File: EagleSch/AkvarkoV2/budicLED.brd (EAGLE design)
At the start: 114.3 x 160 mm, 89 parts, among them IC1 7805T, IC2 4051N, IC3 LF33CV, IC4 ESP01, J1 TRANSFLASH-LOCK, Q1 BD243C, Q2 BD243C, Q3 BD243C, Q4 BD243C, Q5 BC546A, T1 2N5551, T2 2N5551, T3 2N5551, T4 2N5551, U1 ARDUINOR3-DIMENSION, X1 SMKDSP_1,5/2, X2 SMKDSP_1,5/8, X3 SMKDSP_1,5/3

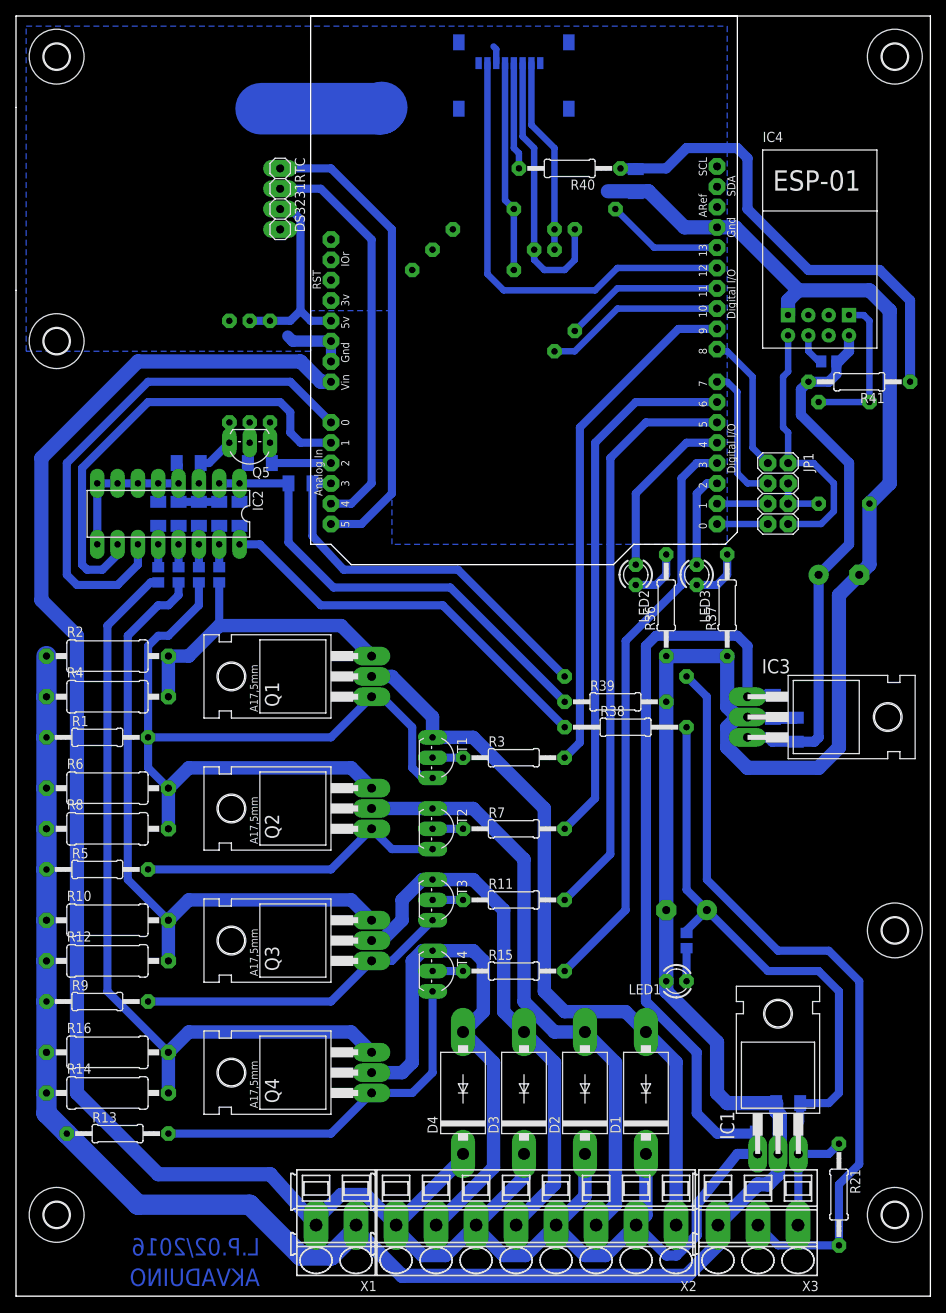
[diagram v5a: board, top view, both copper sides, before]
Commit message: DPS: - RTC modul obracen o 90°, jinak se nevejde do krabicky.
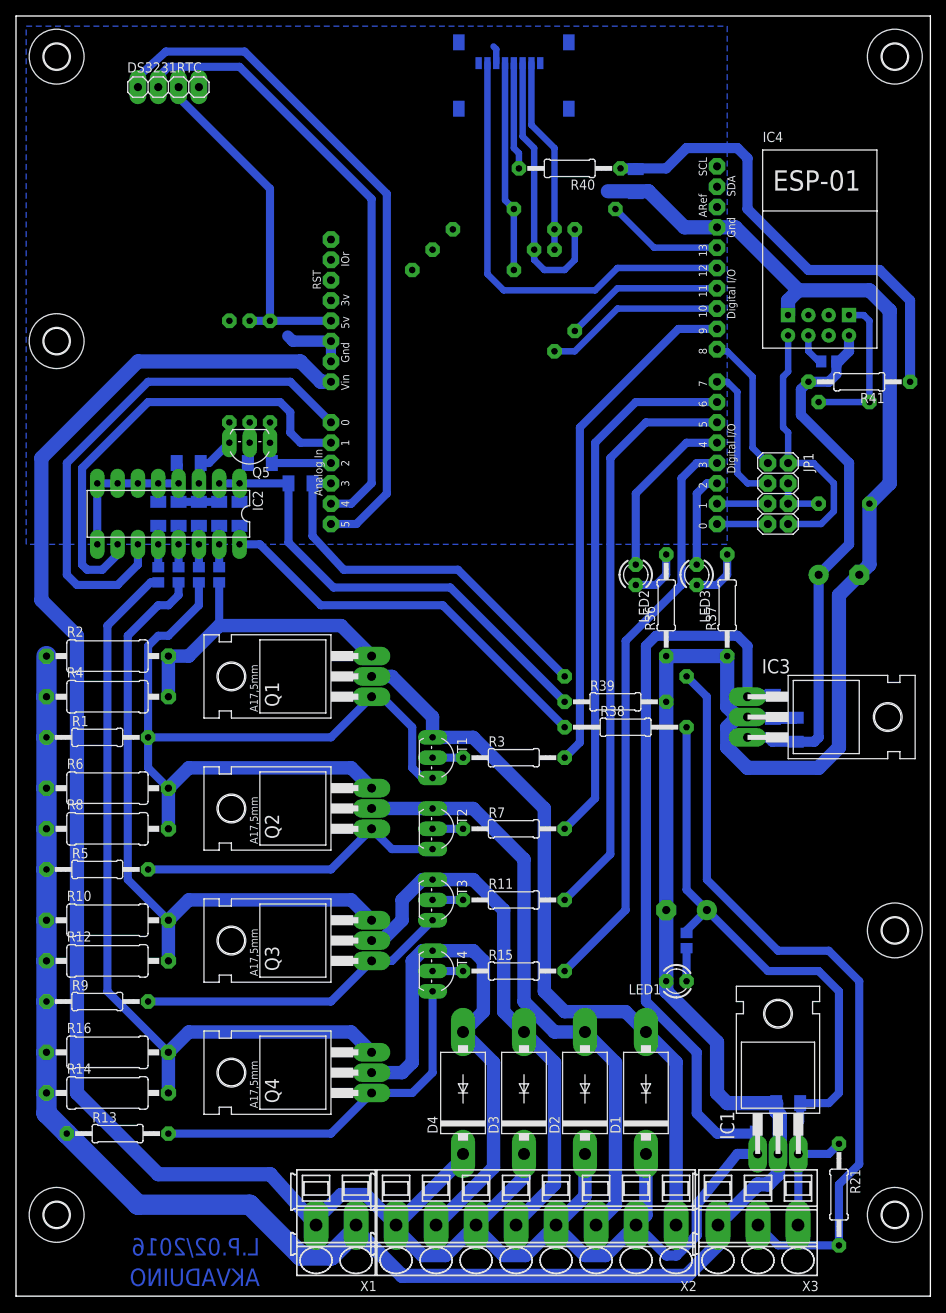
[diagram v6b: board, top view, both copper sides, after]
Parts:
- moved DS3231RTC 19.8 mm to (19.1, 151.1), turned to 0 degrees
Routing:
- net N$13: track 59.3 -> 87.0 mm
- net N$24: track 50.7 -> 77.0 mm
- net N$44: track 25.7 -> 44.1 mm
- net GND: track 412.9 -> 397.7 mm
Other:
- outline, holes or cut-outs redrawn
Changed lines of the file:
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@@
 <wire x1="114.3" y1="0" x2="114.3" y2="160.02" width="0" layer="20"/>
 <wire x1="114.3" y1="160.02" x2="0" y2="160.02" width="0" layer="20"/>
-<wire x1="0" y1="160.02" x2="0" y2="148.59" width="0" layer="20"/>
 <text x="30.48" y="5.08" size="2.1844" layer="16" font="vector" ratio="15" rot="MR0">L.P.02/2016</text>
 <text x="30.48" y="1.27" size="2.1844" layer="16" font="vector" ratio="15" rot="MR0">AKVADUINO</text>
-<wire x1="0" y1="125.73" x2="0" y2="0" width="0" layer="20"/>
-<wire x1="0" y1="125.73" x2="0" y2="148.59" width="0" layer="20"/>
+<wire x1="0" y1="160.02" x2="0" y2="0" width="0" layer="20"/>
 <dimension x1="0" y1="0" x2="114.3" y2="0" x3="57.15" y3="-8.89" textsize="1.778" layer="48"/>
 <dimension x1="114.3" y1="0" x2="114.3" y2="160.02" x3="124.46" y3="80.01" textsize="1.778" layer="48"/>
@@
 <element name="U$4" library="holes" package="3,2" value="" x="5.08" y="119.38"/>
 <element name="IC4" library="esp8266modules" package="ESP01" value="ESP01" x="100.33" y="128.27"/>
-<element name="DS3231RTC" library="pinhead" package="1X04" value="" x="33.02" y="137.16" rot="R270"/>
+<element name="DS3231RTC" library="pinhead" package="1X04" value="" x="19.05" y="151.13"/>
 <element name="U1" library="adafruit" package="ARDUINOR3" value="ARDUINOR3-DIMENSION" x="36.83" y="160.02" rot="R270"/>
 <element name="LED1" library="led" package="LED3MM" value="2.2V 25mA" x="82.55" y="39.37" rot="R180"/>
@@
 <polygon width="0.6096" layer="16">
 <vertex x="88.9" y="93.98"/>
-<vertex x="46.99" y="93.98"/>
-<vertex x="46.99" y="123.19"/>
-<vertex x="36.83" y="123.19"/>
-<vertex x="36.83" y="118.11"/>
-<vertex x="1.27" y="118.11"/>
+<vertex x="1.27" y="93.98"/>
 <vertex x="1.27" y="158.75"/>
 <vertex x="88.9" y="158.75"/>
@@
 <wire x1="79.0575" y1="138.1125" x2="73.9775" y2="138.1125" width="1.778" layer="16"/>
 <wire x1="89.916" y1="133.604" x2="87.63" y2="133.604" width="1.778" layer="16"/>
-<wire x1="30.64" y1="148.43" x2="45.56" y2="148.43" width="6.4516" layer="16"/>
-<wire x1="45.56" y1="148.43" x2="45.72" y2="148.59" width="6.4516" layer="16"/>
 <wire x1="39.37" y1="119.38" x2="34.6075" y2="119.38" width="1.4224" layer="16"/>
 <wire x1="34.6075" y1="119.38" x2="33.9725" y2="120.015" width="1.4224" layer="16"/>
@@
 <wire x1="39.37" y1="99.06" x2="41.91" y2="99.06" width="1.016" layer="16"/>
 <wire x1="41.91" y1="99.06" x2="44.45" y2="101.6" width="1.016" layer="16"/>
-<wire x1="44.45" y1="101.6" x2="44.45" y2="132.08" width="1.016" layer="16"/>
-<wire x1="44.45" y1="132.08" x2="38.1" y2="138.43" width="1.016" layer="16"/>
-<wire x1="38.1" y1="138.43" x2="33.02" y2="138.43" width="1.016" layer="16"/>
+<wire x1="44.45" y1="101.6" x2="44.45" y2="137.16" width="1.016" layer="16"/>
+<wire x1="19.05" y1="153.67" x2="27.94" y2="153.67" width="1.016" layer="16"/>
+<wire x1="27.94" y1="153.67" x2="44.45" y2="137.16" width="1.016" layer="16"/>
+<wire x1="17.78" y1="151.13" x2="17.78" y2="152.4" width="1.016" layer="16"/>
+<wire x1="17.78" y1="152.4" x2="19.05" y2="153.67" width="1.016" layer="16"/>
 </signal>
 <signal name="N$13">
 <contactref element="U1" pad="A5"/>
 <contactref element="DS3231RTC" pad="1"/>
-<wire x1="39.37" y1="96.52" x2="43.18" y2="96.52" width="1.016" layer="16"/>
-<wire x1="43.18" y1="96.52" x2="46.99" y2="100.33" width="1.016" layer="16"/>
-<wire x1="46.99" y1="100.33" x2="46.99" y2="133.35" width="1.016" layer="16"/>
-<wire x1="46.99" y1="133.35" x2="39.37" y2="140.97" width="1.016" layer="16"/>
-<wire x1="39.37" y1="140.97" x2="33.02" y2="140.97" width="1.016" layer="16"/>
+<wire x1="39.37" y1="96.52" x2="42.545" y2="96.52" width="1.016" layer="16"/>
+<wire x1="42.545" y1="96.52" x2="46.355" y2="100.33" width="1.016" layer="16"/>
+<wire x1="46.355" y1="100.33" x2="46.355" y2="137.795" width="1.016" layer="16"/>
+<wire x1="15.24" y1="151.13" x2="15.24" y2="152.4" width="1.016" layer="16"/>
+<wire x1="15.24" y1="152.4" x2="18.7325" y2="155.575" width="1.016" layer="16"/>
+<wire x1="18.7325" y1="155.575" x2="28.575" y2="155.575" width="1.016" layer="16"/>
+<wire x1="28.575" y1="155.575" x2="46.355" y2="137.795" width="1.016" layer="16"/>
 </signal>
 <signal name="SCK">
@@
 <contactref element="DS3231RTC" pad="3"/>
 <contactref element="U1" pad="5V"/>
-<wire x1="39.37" y1="121.92" x2="36.83" y2="121.92" width="1.016" layer="16"/>
-<wire x1="36.83" y1="121.92" x2="35.56" y2="123.19" width="1.016" layer="16"/>
-<wire x1="35.56" y1="123.19" x2="35.56" y2="134.62" width="1.016" layer="16"/>
-<wire x1="35.56" y1="134.62" x2="34.29" y2="135.89" width="1.016" layer="16"/>
-<wire x1="34.29" y1="135.89" x2="33.02" y2="135.89" width="1.016" layer="16"/>
 <contactref element="R34" pad="1"/>
 <wire x1="29.21" y1="121.92" x2="31.75" y2="121.92" width="1.016" layer="16"/>
-<wire x1="31.75" y1="121.92" x2="34.29" y2="121.92" width="1.016" layer="16"/>
-<wire x1="34.29" y1="121.92" x2="35.56" y2="123.19" width="1.016" layer="16"/>
+<wire x1="39.37" y1="121.92" x2="31.75" y2="121.92" width="1.016" layer="16"/>
+<wire x1="31.75" y1="138.43" x2="31.75" y2="121.92" width="1.016" layer="16"/>
+<wire x1="31.75" y1="138.43" x2="20.32" y2="149.86" width="1.016" layer="16"/>
+<wire x1="20.32" y1="149.86" x2="20.32" y2="151.13" width="1.016" layer="16"/>
 </signal>
 <signal name="N$19">

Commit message: DPS: - vytvorena objednavka soucastek v GME
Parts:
- C14: value 330n -> 100n
- C9: value 100n -> 330n
- R22: value 390R -> 1k
- R23: value 4k7 -> 1k
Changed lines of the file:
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@@
 <element name="U1" library="adafruit" package="ARDUINOR3" value="ARDUINOR3-DIMENSION" x="36.83" y="160.02" rot="R270"/>
 <element name="LED1" library="led" package="LED3MM" value="2.2V 25mA" x="82.55" y="39.37" rot="R180"/>
-<element name="R22" library="rcl" package="R0805" value="390R" x="83.82" y="44.45" rot="MR270"/>
+<element name="R22" library="rcl" package="R0805" value="1k" x="83.82" y="44.45" rot="MR270"/>
 <element name="C10" library="resistor" package="E5-10,5" value="CE 1000u/35VIT" x="102.87" y="90.17" rot="MR180"/>
 <element name="IC3" library="linear" package="TO220H" value="LF33CV" x="104.14" y="72.39" rot="R270"/>
-<element name="C9" library="rcl" package="C1206K" value="100n" x="94.615" y="73.66" rot="MR270"/>
+<element name="C9" library="rcl" package="C1206K" value="330n" x="94.615" y="73.66" rot="MR270"/>
 <element name="C8" library="rcl" package="C1206K" value="100n" x="97.4725" y="70.8025" rot="MR90"/>
 <element name="U$5" library="holes" package="3,2" value="" x="109.855" y="154.94"/>
 <element name="IC2" library="40xx" package="DIL16" value="4051N" x="19.05" y="97.79" rot="R180"/>
 <element name="C11" library="rcl" package="C1206K" value="330n" x="21.59" y="104.14" rot="MR0"/>
-<element name="R23" library="rcl" package="R0805" value="4k7" x="101.6" y="116.84" rot="MR0"/>
+<element name="R23" library="rcl" package="R0805" value="1k" x="101.6" y="116.84" rot="MR0"/>
 <element name="R24" library="rcl" package="0207/15" value="4k7" x="76.2" y="77.47" rot="MR0"/>
 <element name="C12" library="rcl" package="C1206K" value="330n" x="35.56" y="101.6" rot="MR0"/>
@@
 <element name="R34" library="rcl" package="0207/12" value="10k" x="29.21" y="115.57" rot="MR270"/>
 <element name="R35" library="rcl" package="0207/12" value="10k" x="26.67" y="115.57" rot="MR90"/>
-<element name="C14" library="rcl" package="C1206K" value="330n" x="30.48" y="104.14" rot="MR0"/>
+<element name="C14" library="rcl" package="C1206K" value="100n" x="30.48" y="104.14" rot="MR0"/>
 <element name="LED2" library="led" package="LED3MM" value="2.2V 25mA" x="77.47" y="90.17" rot="R270"/>
 <element name="LED3" library="led" package="LED3MM" value="2.2V 25mA" x="85.09" y="90.17" rot="R270"/>

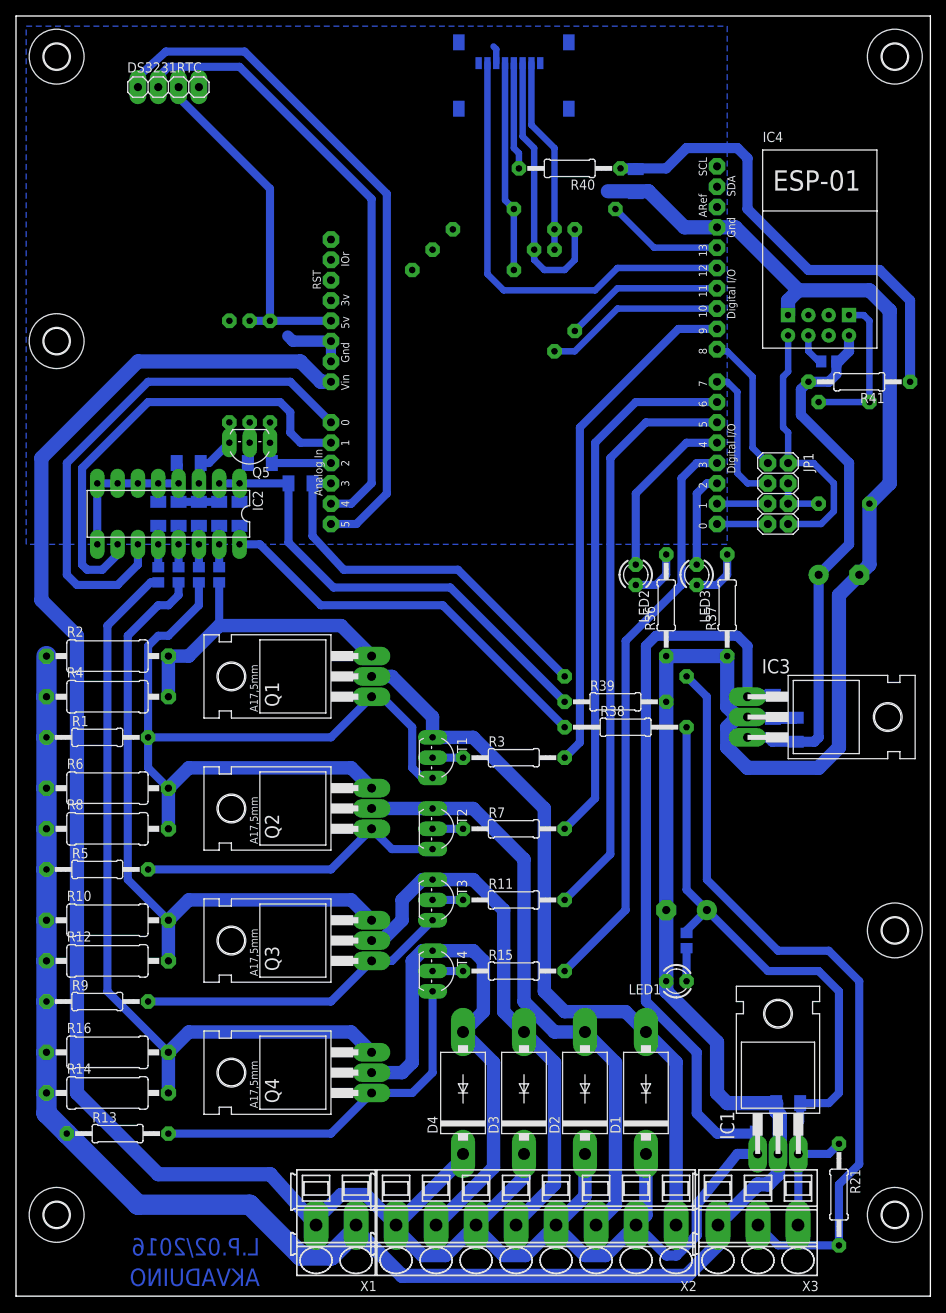
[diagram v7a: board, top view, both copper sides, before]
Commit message: DPS: - opraven chybejici propoj - opraveno zrcadleni soucastek
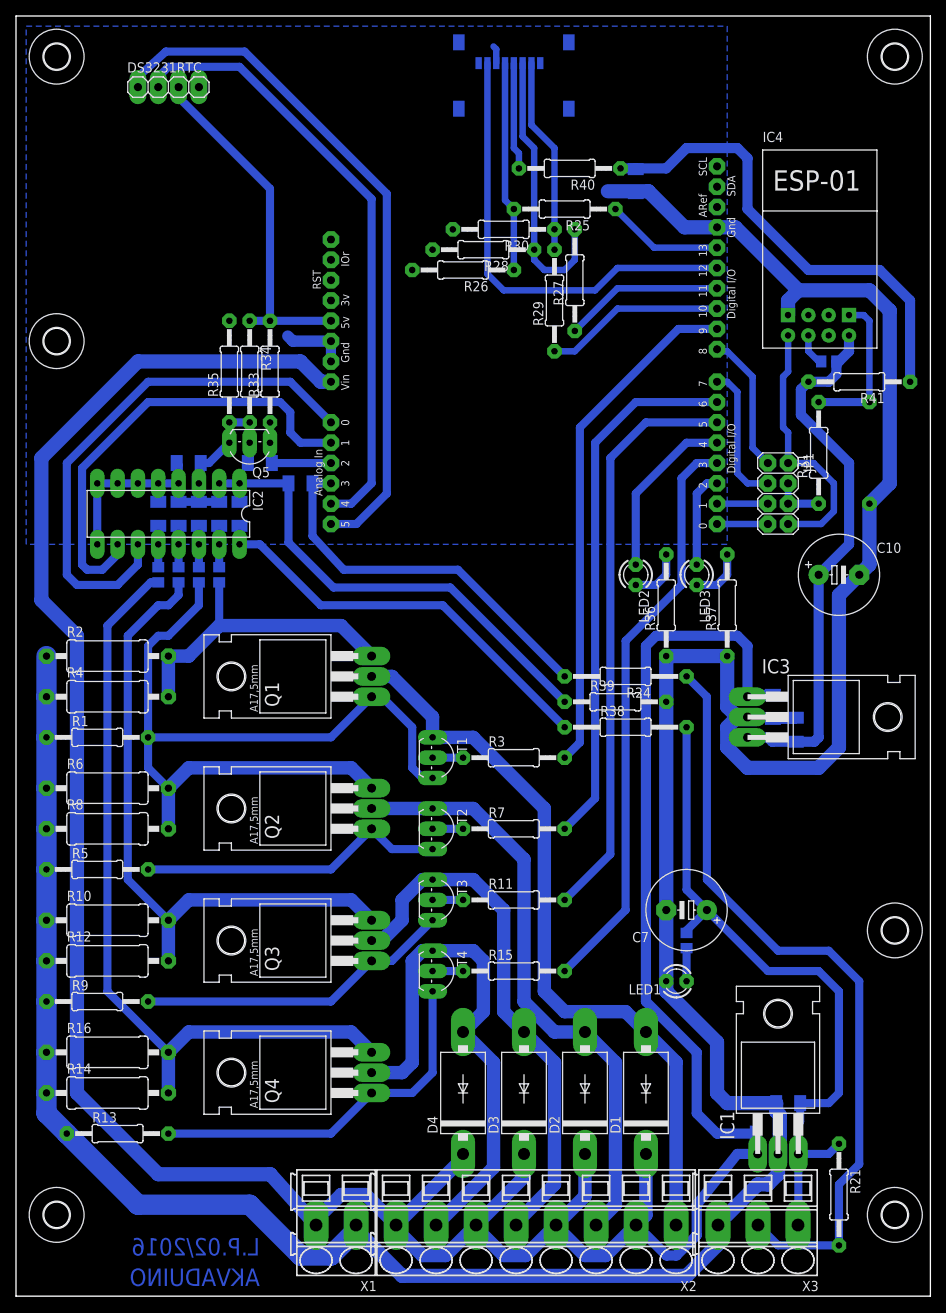
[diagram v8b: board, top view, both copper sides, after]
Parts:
- flipped C10 to the top, turned to 0 degrees
- flipped C7 to the top, turned to 180 degrees
- flipped R24 to the top, turned to 180 degrees
- flipped R25 to the top, turned to 180 degrees
- flipped R26 to the top, turned to 180 degrees
- flipped R27 to the top
- flipped R28 to the top, turned to 180 degrees
- flipped R29 to the top
- flipped R30 to the top, turned to 180 degrees
- flipped R31 to the top
- flipped R33 to the top
- flipped R34 to the top
- flipped R35 to the top
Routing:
- net N$19: track 5.16 -> 7.70 mm
